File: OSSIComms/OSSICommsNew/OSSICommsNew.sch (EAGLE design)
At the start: 158 parts, among them Q2 NX-3215, U1 PCA9548APWR, U10 MAX6369, U11 OPA4347, U13 SN65HVD11QD, U14 LTC4411, U15 MCP1700_SOT23, U16 DS3231-L, U17 FM24V02-G, U18 TMP101, U19 24LC256-8LEAD, U2 ADG708, U20 LTC4411, U21 SN74LVC8T245PWR, U23 ADXRS450SOIC, U3 MAX890L, U4 OPA4347, U5 MSP430F1611, U6 OPA4347, U7 TPS3838, U8 ADG708, U9 ADR121, X1 ESQ-126-38-G-D, X2 JTAG10PINMINI-H, X3 MOLEX-22-05-7045, X5 P-PAD-S, X6 P-PAD-S

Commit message: ossi comms new added
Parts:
- removed BAT1: BATTERY-BH32T, OSSI:BATTERY-BH32T
- removed D1: MMSD4148T1G, OSSI:MMSD4148T1G
- removed R44, R58, R60, R64, R65: 470k, OSSI:R0603(1608)
- removed R45, R52, R57, R59, R61, R63, R66: 4.7k, OSSI:R0603(1608)
- removed R46, R47, R48, R49, R50, R51, R53, R54, R55, R69, R70: 1.5k, OSSI:R0603(1608)
- removed R56, R62, R68, R71, R72, R73: 10k, OSSI:R0603(1608)
- removed R67: 300k, OSSI:R0603(1608)
- removed R74: 100k, OSSI:R0603(1608)
- removed R76, R77: 0, OSSI:R0603(1608)
- removed TR2: FDV301N, OSSI:FDV301N
- removed U13: SN65HVD11QD, OSSI:SN65HVD11QD
- removed U15: MCP1700_SOT23, OSSI:MCP1700_SOT23
- removed U17: FM24V02-G, OSSI:FM24V02-G
- removed U18: TMP101, OSSI:TMP101
- removed U19: 24LC256-8LEAD, OSSI:24LC256-8LEAD
- removed U20: LTC4411, OSSI:LTC4411
- removed U21: SN74LVC8T245PWR, OSSI:SN74LVC8T245PWR
- removed U23: ADXRS450SOIC, OSSI:ADXRS450SOIC
- added C35, C44, C47, C55, C65, C67, C68, C70, C71: 100nF, OSSI:C0603(1608)
- added C43, C46: 1.2nF, OSSI:C0603(1608)
- added C45, C48, C54, C63, C74, C75, C87, C88, C89, C96: 10nF, OSSI:C0603(1608)
- added C49: 6.8pF, OSSI:C0603(1608)
- added C50, C51, C56, C57, C66: DNP, OSSI:C0603(1608)
- added C52, C53, C69: (no value), OSSI:C0603(1608)
- added C58, C72: 22uF,1210, OSSI:C1210(3225)-GCM32
- added C59, C60, C61: (no value), OSSI:C1210(3225)-GCM32
- added C62: 100uF,1210, OSSI:C0805(2012)
- added C64: 180pF, OSSI:C0603(1608)
- added C78, C79, C84: 22pF, OSSI:C0603(1608)
- added C80: 8.2pF, OSSI:C0603(1608)
- added C81: 47pF, OSSI:C0603(1608)
- added C82, C91, C95: 1nF, OSSI:C0603(1608)
- added C83, C90: 3.3uF, OSSI:C1210(3225)-TMK325
- added C85: 2pF, OSSI:C0603(1608)
- added C86: 56pF, OSSI:C0603(1608)
- added C92: 10pF, OSSI:C0603(1608)
- added C93: 15pF, OSSI:C0603(1608)
- added C94: 330pF, OSSI:C0603(1608)
- added JP2: (no value), OSSI:JP1Q
- added L10, L14, L15, L7, L8, L9: (no value), OSSI:L0603(1608)
- added L11: 3.9nH, OSSI:L0603(1608)
- added L12: 1.5nH, OSSI:L0603(1608)
- added L13: 0 Ohm, OSSI:L0805(2012)
- added L16: 330uH, OSSI:LLQH32CN
- added L2, L3: 11nH, OSSI:L0603(1608)
- added L4: 27nH, OSSI:L0603(1608)
- added L5: 39nH 3012, 1A rating, OSSI:LNR3012
- added L6: 47nH, OSSI:L0603(1608)
- added LED2: (no value), led:LEDCHIPLED_0603
- added TCXO2, TCXO3: 19.2MHz, OSSI:TCXO-M532
- added TP1: TP, OSSI:TP
- added TR1: FDV301N, OSSI:FDV301N
- added X7: 5268-03, OSSI:5268-03
- C11: value 100nF -> 470pF 0805; device OSSI:C0603(1608) -> OSSI:C0805(2012)
- C12: value 100nF -> 10uF; device OSSI:C0603(1608) -> OSSI:C1206(3216)-GCM31
- C15, C17, C19, C26, C28: value 100nF -> 10nF
- C2, C6: value 100nF -> 13pF
- C20, C31: value 100nF -> 22nF
- C23: value 100nF -> 100pF
- C29, C32: value 1uF 0805 -> 100nF; device OSSI:C0805(2012) -> OSSI:C0603(1608)
- C30: value 1uF 0805 -> 10nF; device OSSI:C0805(2012) -> OSSI:C0603(1608)
- C34: value 10uF, LDO Tantal 16V -> 100pF; device OSSI:C-TANTAL-A -> OSSI:C0603(1608)
- C37: value 10uF,3225 -> 100nF; device OSSI:C1210(3225)-GCM32 -> OSSI:C0603(1608)
- C38: value 4.7uF, 1210 -> 100pF; device OSSI:C1206(3216)-GCM31 -> OSSI:C0603(1608)
- C39: value 100nF -> 15pF
- C4, C5: value 100nF -> 10uF, LDO Tantal 16V; device OSSI:C0603(1608) -> OSSI:C-TANTAL-A
- C40: value 100nF -> 8.2pF
- C41: value 100nF -> 12pF
- C42: value 10uF, LDO Tantal 16V -> 8.2pF; device OSSI:C-TANTAL-A -> OSSI:C0603(1608)
- C9: value 100nF -> 1500pF
- F1: value POLYSWITCH -> LFCN-530; device OSSI:POLYSWITCH -> OSSI:LFCN-160
- L1: value 470uH, 240mA -> 26nH; device OSSI:LQH55 -> OSSI:L0603(1608)
- LED1: device SparkFun:LED0603 -> led:LEDCHIPLED_0603
- R10: value 10k -> 3.6k
- R11: value 10k -> 3.9
- R12: value 33k -> 1.1k
- R13: value 33k -> 3.6k
- R14: value 100k -> 3.9
- R15, R17: value 100k -> 280
- R16, R18: value 100k -> 100
- R19, R6, R7: value 100k -> 1.5k
- R21: value 10k -> 15.968k
- R22: value 250 -> 49.9k
- R23: value 250 -> 4.12k
- R24: value 250 -> TBD
- R25, R33: value 250 -> 1.5k
- R28, R32: value 250 -> 100k
- R29: value 250 -> 1k
- R34: value 4.7k -> 180
- R35: value 120, DNP -> 470k
- R36: value 10k -> 11nH
- R37: value 10k -> 22k
- R38: value 10k -> 100k
- R39: value 10k -> 1k
- R4: value 100k -> 470k
- R40, R5: value 10k -> 4.7k
- R41, R43: value 100k -> 4.7k
- R42: value 1.5k -> 4.7k
- R9: value 100k -> 1.1k
- U1: value PCA9548APWR -> MAX890L; device OSSI:PCA9548APWR -> OSSI:MAX890L
- U10: value MAX6369 -> LMZ10503EXT; device OSSI:MAX6369 -> OSSI:LMZ10503EXT
- U11: value OPA4347 -> OPA347; device OSSI:OPA4347 -> OSSI:OPA347
- U14: value LTC4411 -> RF5110G; device OSSI:LTC4411 -> OSSI:RF5110G
- U16: value DS3231-L -> MAX2640; device OSSI:DS3231-L -> OSSI:MAX2640
- U2: value ADG708 -> ADF7021-N; device OSSI:ADG708 -> OSSI:ADF7021-N
- U3: value MAX890L -> ADF7021-N; device OSSI:MAX890L -> OSSI:ADF7021-N
- U4: value OPA4347 -> PE4259; device OSSI:OPA4347 -> OSSI:PE4259
- U6: value OPA4347 -> MAX6369; device OSSI:OPA4347 -> OSSI:MAX6369
- U8: value ADG708 -> MCP1700_SOT23; device OSSI:ADG708 -> OSSI:MCP1700_SOT23
- U9: value ADR121 -> MAX869L; device OSSI:ADR127BUJZ-REEL7 -> OSSI:MAX869L
- X3: value MOLEX-22-05-7045 -> P-PAD-S; device OSSI:MOLEX-22-05-7045 -> OSSI:P-PAD-S
- X4: value (none) -> P-PAD-S; device OSSI:M03PTH -> OSSI:P-PAD-S
- X5: value P-PAD-S -> RFCON-MCX-R/A; device OSSI:P-PAD-S -> OSSI:RFCON-MCX-R/A
- X6: value P-PAD-S -> (none); device OSSI:P-PAD-S -> OSSI:M03PTH
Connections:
- net RESETOBC renamed /RST
- removed net /RE: R12.1, TR2.D, U13.P$2
- removed net 3.3VOBC_I2C: C18.1, C19.1, C20.1, C21.1, R5.2, R64.2, R65.1, R72.2, U14.P$5, U16.P$2, U17.A0, U17.VDD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
- removed net A: R35.2, U13.P$6, X3.2
- removed net ADC0: C5.1, R10.1, U5.59
- removed net ADC1: C9.1, R11.1, U5.60
- removed net B: R35.1, U13.P$7, X3.3
- removed net BAT_-CHRG_IN: R48.2, U5.17
- removed net BAT_-FAULT_IN: R49.2, U5.16
- removed net BAT_-ON_IN: R46.2, U5.19
- removed net BEACON_-FAULT_IN: R59.2, U5.22
- removed net BEACON_OFF_OUT: R54.2, U5.38
- removed net COMMS_-FAULT_IN: R61.2, U5.21
- removed net COMMS_OFF_OUT: R55.2, U5.37
- removed net DE: R13.2, U13.P$3, U5.48
- removed net GYRO_-CS: U23.P$4, U5.44
- removed net GYRO_SCLK: U23.P$16, U5.47
- removed net GYRO_SI: U23.P$15, U5.45
- removed net GYRO_SO: U23.P$5, U5.46
- removed net I2C_-RST: R4.1, U1.P$3, U5.28
- removed net I2C_SCL: R26.1, R30.1, U1.P$22
- removed net I2C_SCL_TP: R26.2, U5.31, X4.2
- removed net I2C_SDA: R27.1, R31.1, U1.P$23
- removed net I2C_SDA_TP: R27.2, U5.29, X4.1
- removed net IO_-OE: R43.1, U21.P$22, U5.24
- removed net LED_-FAULT_IN: R57.2, U5.23
- removed net LED_OFF_OUT: R53.2, U5.39
- removed net MUX_A0: R76.2, U2.P$1, U8.P$1
- removed net MUX_A1: R77.2, U2.P$16, U8.P$16
- removed net MUX_A2: U2.P$15, U5.51, U8.P$15
- removed net N$2 (its old number): R7.1, R9.2, U4A.+IN
- removed net N$666: C3.1, C34.+, U15.3, U3.P$6, U3.P$7
- removed net N$82: D1.A, L1.2, U23.P$8
- removed net N$90: C31.2, D1.C, U23.P$9
- removed net OBC_I2C_OFF: R74.1, U14.P$3, U5.30
- removed net OBC_SCL: R23.1, R24.1, R28.1, R33.1, R72.1, U1.P$14
- removed net OBC_SDA: R22.1, R25.1, R29.1, R32.1, R5.1, U1.P$13
- removed net OBC_WT_RST: C4.1, U10.P$7, U7.P$3
- removed net RTC_-INT: R64.1, U16.P$3, U5.26
- removed net RXD1: R34.1, U5.35
- removed net SCCHG_EN_OUT: R69.2, U5.41
- removed net SCOUT_-PG_IN: R51.2, U5.14
- removed net SCOUT_EN_OUT: R70.2, U5.40
- removed net SC_-ON_IN: R47.2, U5.18
- removed net SC_-PFO_IN: R50.2, U5.15
- removed net SOLAR_-ON_IN: R42.2, U5.20
- removed net STATUS_LED: JP1.2, LED1.A, R66.1
- removed net SUN_IN: U11B.-IN, U11B.OUT, U8.P$11
- removed net TEMP_-ALERT: R65.2, U18.3, U5.27
- removed net TXD1: R63.1, U5.34
- removed net VEXT: C37.1, F1.P$2, R6.1, U20.P$1
- removed net VEXT_OFF: R20.1, U20.P$3, U5.36
- removed net VREF_EXT: C33.2, U5.10, U9.P$4
- new net 3.3VCOMMS: C5.+, C54.1, C7.1, C70.1, C72.1, C8.1, L13.1, R2.2, R28.1, R30.2, R31.2, R4.2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
- new net COMMSRX_CE: U3.P$24, U5.21
- new net COMMSRX_CLK: R42.2, U3.P$35
- new net COMMSRX_CLKOUT: U3.P$36
- new net COMMSRX_CPOUT: C45.1, R15.2, R16.2, U3.P$42
- new net COMMSRX_DATA: R43.2, U3.P$34
- new net COMMSRX_MUXOUT: U3.P$37, U5.13
- new net COMMSRX_RFIN: C2.1, L4.2, U3.P$6
- new net COMMSRX_RFINB: C49.1, L4.1, U3.P$7
- new net COMMSRX_SCLK: U3.P$28, U5.17
- new net COMMSRX_SDATA: U3.P$26, U5.19
- new net COMMSRX_SLE: U3.P$25, U5.20
- new net COMMSRX_SREAD: U3.P$27, U5.18
- new net COMMSRX_SWD: U3.P$33, U5.16
- new net COMMSRX_TCXO: C79.2, U3.P$39
- new net COMMSRX_VCOIN: C43.1, R15.1, U3.P$1
- new net COMMSTX_CE: U2.P$24, U5.37
- new net COMMSTX_CLK: R41.2, U2.P$35
- new net COMMSTX_CLKOUT: U2.P$36
- new net COMMSTX_CPOUT: C48.1, R17.2, R18.2, U2.P$42
- new net COMMSTX_DATA: R40.2, U2.P$34
- new net COMMSTX_MUXOUT: U2.P$37, U5.22
- new net COMMSTX_RFOUT: C6.1, L1.1, U2.P$4
- new net COMMSTX_SCLK: U2.P$28, U5.25
- new net COMMSTX_SDATA: U2.P$26, U5.27
- new net COMMSTX_SLE: U2.P$25, U5.36
- new net COMMSTX_SREAD: U2.P$27, U5.26
- new net COMMSTX_TCXO: C78.2, U2.P$39
- new net COMMSTX_VCOIN: C46.1, R17.1, U2.P$1
- new net COMMS_-RST: C71.1, U6.P$7, U7.P$3
- new net LED1: R39.1, U5.50
- new net N$23: C51.2, L7.2, L8.1
- new net N$63: R43.1, U5.15
- new net N$66: C79.1, TCXO3.P$3
- new net N$67: R40.1, U5.24
- new net N$68: C78.1, TCXO2.P$3
- new net N$69: U5.42, U6.P$1
- new net N$73: C80.2, U14.P$3
- new net N$74: C5.-, R75.1
- new net N$75: L11.1, L5.1, U14.P$10, U14.P$11, U14.P$12, U14.P$9
- new net N$76: JP1.2, U11.OUT
- new net N$77: U5.33, X3.P$1
- new net N$78: U5.32, X4.P$1
- new net N$79: C93.1, L12.1, L16.2
- new net N$80: R36.1, U14.P$1
- new net OBC_-FAULT_IN: R5.1, U5.12
- new net OBC_OFF_OUT: R7.1, U5.2
- new net PA_-FAULT: R28.2, U9.P$10
- new net PA_BIAS: R33.1, R37.2, R38.1, U5.5
- new net PA_ON: R25.2, R35.1, U5.40
- new net RX_ON: U5.39
- new net STRUT_GND: H1.MOUNT
- new net TX_ON: R32.2, R6.1, U5.38
- new net VAPC: C88.2, C89.2, JP1.1, U14.P$15, U14.P$16
- new net VCCRF: C11.1, C12.1, C15.1, C17.1, C19.1, C22.1, C23.1, C24.1, C26.1, C28.1, C30.1, C33.1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
- new net VCOMMS_PA: C59.1, C60.1, C62.1, C64.1, C68.1, C81.1, C82.1, C83.1, C87.2, C90.1, C91.1, C92.1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
- net 3.3VOBC: no longer C11.1, C12.1, C15.1, C16.1, C17.2, C2.1, C27.1, C28.1, C30.1, C42.+, C6.1, C7.1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
- net ANT_DEPLOY1: no longer R45.1
- net ANT_DEPLOY2: no longer R52.1
- net BAT_-CHRG: no longer U21.P$18
- net BAT_-FAULT: no longer U21.P$17
- net BAT_-ON: no longer U21.P$20
- net BAT_TEMP: no longer R68.2
- net BEACON_-FAULT: no longer R58.1, R59.1
- net BEACON_OFF: no longer R54.1
- net BEACON_SCL: no longer U1.P$7
- net BEACON_SDA: no longer U1.P$6
- net BUS_CS: no longer R40.2
- net COMMS_-FAULT: now also U1.P$8; no longer R60.1, R61.1
- net COMMS_OFF: now also C1.1, R3.2, U1.P$3; no longer R55.1
- net COMMS_SCL: now also R26.1, R30.1, X6.2; no longer U1.P$5
- net COMMS_SDA: now also R27.1, R31.1, X6.1; no longer U1.P$4
- net GND: now also C17.2, C33.2, C34.2, C35.2, C4.-, C42.2, C43.2, C44.2, C45.2, C46.2, C47.2, C48.2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; no longer BAT1.-, C17.1, C2.2, C20.2, C21.2, C31.1, C32.2, C33.1, C34.-, C39.2, C4.2, C5.2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
- net LED_-FAULT: no longer R44.1, R57.1
- net LED_OFF: no longer R53.1
- net LED_SCL: no longer U1.P$9
- net LED_SDA: no longer U1.P$8
- net N$1: now also C16.1, U3.P$41; no longer U10.P$1, U5.12
- net N$10: now also C25.1, U3.P$11; no longer R1.2, U3.P$5
- net N$11: now also C3.1, C4.+, U1.P$6, U1.P$7, U8.3; no longer U2.P$4, U4D.-IN, U4D.OUT
- net N$12: now also R1.2, U1.P$5; no longer U6A.-IN, U6A.OUT, U8.P$7
- net N$14: now also C39.2, U16.4; no longer R34.2, U13.P$1
- net N$15: now also C50.1, F1.P$1, L9.1; no longer R33.2, U16.P$16
- net N$16: now also C9.2, F1.P$3; no longer R73.1, U1.P$15, U1.P$16, U1.P$17, U1.P$18, U1.P$19, U1.P$20
- net N$21: now also C53.1, L10.1, L9.2; no longer U6B.-IN, U6B.OUT, U8.P$6
- net N$22: now also C20.1, U3.P$48; no longer R63.2, U13.P$4
- net N$24: now also R9.1, U3.P$8; no longer R14.1, R15.2, U4B.+IN
- net N$25: now also R10.1, U3.P$10; no longer R16.1, R17.2, U4C.+IN
- net N$26: now also C21.2, R11.2; no longer R18.1, R19.2, U4D.+IN
- net N$27: now also C31.1, U2.P$48; no longer R11.2, U2.P$8
- net N$28: now also R13.2, U2.P$10; no longer U6C.-IN, U6C.OUT, U8.P$5
- net N$29: now also C32.2, R14.2; no longer R10.2, U8.P$8
- net N$3: now also C36.1, U2.P$11; no longer U2.P$7, U4A.-IN, U4A.OUT
- net N$30: now also R12.2, U2.P$8; no longer U6D.-IN, U6D.OUT, U8.P$4
- net N$31: now also C27.1, U2.P$41; no longer U11A.-IN, U11A.OUT, U8.P$12
- net N$32: now also C29.1, U2.P$31; no longer R66.2, U5.13
- net N$33: now also C42.1, C80.1, L3.2, R34.2; no longer C32.1, U23.P$1
- net N$34: now also C31.2, C32.1, U2.P$2; no longer R29.2, U19.P$5
- net N$35: now also C20.2, C21.1, U3.P$2; no longer R28.2, U19.P$6
- net N$36: now also C40.1, C6.2, L2.1; no longer R25.2, U17.SDA
- net N$37: now also C41.1, L2.2, L3.1; no longer R45.2, U5.43
- net N$38: now also C47.1, R18.1; no longer R52.2, U5.42
- net N$39: now also C52.2, C57.2, L8.2; no longer R24.2, U17.SCL
- net N$4: now also C56.2, C86.2, L7.1; no longer R41.1, R6.2, TR2.G
- net N$40: now also C44.1, R16.1; no longer R22.2, U18.6
- net N$41: now also C69.2, U4.P$5; no longer R23.2, U18.1
- net N$42: now also R6.2, U4.P$4; no longer R67.2, U5.25
- net N$43: now also C39.1, L14.2, L15.1; no longer C36.1, F1.P$1, X3.1
- net N$44: now also R19.1, U4.P$6; no longer U11C.-IN, U11C.OUT, U8.P$10
- net N$45: now also LED2.A, R29.2; no longer U11D.-IN, U11D.OUT, U8.P$9
- net N$46: now also C69.1, X5.1; no longer C29.1, U23.P$14
- net N$47: now also C65.1, R20.1, TR1.D, U9.P$7; no longer C41.1, R71.1, U11D.+IN
- net N$48: now also R29.1, U5.49; no longer C40.1, R68.1, U11C.+IN
- net N$49: now also JP2.1, LED1.A, R39.2; no longer R48.1, U21.P$6
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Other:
- note added: "0.8Vpp out with ac coupled capacitor"
- note added: "0dbm"
- note added: "1Watt"
- note added: "50 Ohm"
- note added: "75 Ohm"
- note added: "C value?"
- note added: "DIGITAL / RF POWER CHOKE"
- note added: "Harmonics Filter"
- note added: "LC Balun"
- note added: "Maching"
- note added: "OPEN SOURSE SATELLITE INITIATIVE Ver 0.9"
- note added: "PA Maching"
- note added: "Power Amplifier"
- note added: "Tantal Cap should be used"
- note added: "Use DAC to change the divider voltage point"
- note added: "also check 23.7k / 75k combination"
- note added: "chage this if resistance affects"
- note added: "clkout testpoint"
- note added: "for VAPC of PA"
- note added: "important!!"
- note added: "post impedance matching"
- note added: "pull down!!"
- note added: "set to 2.8V"
- note added: "sync word detection eyediagram test?"
- note added: "unconnected pins?"
- note added: "variable capacitor"
- note removed: "/RE needs to go LOW when external interface connector is inserted"
- note removed: "12pF"
- note removed: "60s time set"
- note removed: "All pull up to VBUS"
- note removed: "But can be turned off by OBC for testing"
- note removed: "DE pin to OBC"
- note removed: "EN is Active High"
- note removed: "Max Current: 1.2A"
- note removed: "OBC pull high DE pin when TX"
- note removed: "ROSC for better DCO"
- note removed: "Ref1: Poly Sat paper"
- note removed: "Ref2: Pumpkin Co. Cubesat kit"
- note removed: "Remove 0 Ohm for SMCLK / ACLK out"
- note removed: "VEXT On by default to charge the battery from VEXT"
- note removed: "VEXT will turn on the 485 in Receiver mode"
- note removed: "Vout Overshoot check"
- note removed: "changed from 0 -> 1k"
- note removed: "critical signal should be directly connect to MCU"
- note removed: "input to OBC"
- note removed: "interface side select power from Solar or 5V adaptor"
- note removed: "led"
- note removed: "output capacitor!"
- note removed: "output capacitor!!!"
- note removed: "output from OBC"
- note removed: "power capacitors"
- note removed: "put 1k resistor at the output of current sensor"
- note removed: "sun sensor"
- note removed: "unused pins!!"
- note removed: "write enabled"

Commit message: beta 1 release
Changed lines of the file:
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@@
 <part name="GND60" library="OSSI" deviceset="GND" device=""/>
 <part name="3.3VCOMMS17" library="OSSI" deviceset="3.3VCOMMS" device=""/>
-<part name="VCCRF1" library="OSSI" deviceset="VCCRF" device=""/>
 <part name="VCCRF3" library="OSSI" deviceset="VCCRF" device=""/>
 <part name="VCCRF4" library="OSSI" deviceset="VCCRF" device=""/>
@@
 <instance part="GND58" gate="1" x="220.98" y="210.82"/>
 <instance part="GND59" gate="1" x="220.98" y="76.2"/>
-<instance part="VCCRF1" gate="G$1" x="17.78" y="149.86"/>
 <instance part="VCCRF5" gate="G$1" x="101.6" y="81.28"/>
 <instance part="VCCRF6" gate="G$1" x="261.62" y="71.12"/>

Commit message: schematics renumbered
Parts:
- removed C94: 330pF, OSSI:C0603(1608)
- removed C95: 1nF, OSSI:C0603(1608)
- removed C96: 10nF, OSSI:C0603(1608)
- removed R75: 0, OSSI:R0603(1608)
- removed U14: RF5110G, OSSI:RF5110G
- removed U16: MAX2640, OSSI:MAX2640
- added C73, C77: 100nF, OSSI:C0603(1608)
- added C76: 10nF, OSSI:C0603(1608)
- added R44: 100k, OSSI:R0603(1608)
- added U12: MAX890L, OSSI:MAX890L
- added U13: MCP1700_SOT23, OSSI:MCP1700_SOT23
- C1: value 1uF -> 6.8pF
- C10: value 100nF -> (none)
- C11: value 470pF 0805 -> 3.3uF; device OSSI:C0805(2012) -> OSSI:C1210(3225)-TMK325
- C12: value 10uF -> 10pF; device OSSI:C1206(3216)-GCM31 -> OSSI:C0603(1608)
- C13: value 12.5pF -> 1nF
- C14: value 12.5pF -> 15pF
- C15: value 10nF -> (none)
- C16: value 100nF -> DNP
- C17: value 10nF -> DNP
- C18, C25: value 100nF -> 8.2pF
- C19: value 10nF -> 12pF
- C2: value 13pF -> DNP
- C20: value 22nF -> 8.2pF
- C21: value 100nF -> 22pF
- C22: value 100nF -> 2pF
- C23: value 100pF -> DNP
- C24, C3: value 100nF -> 13pF
- C26: value 10nF -> 56pF
- C27: value 100nF -> 330pF
- C29, C70: value 100nF -> 100pF
- C30: value 10nF -> 47pF
- C31: value 22nF -> 1nF
- C32, C35, C36, C67: value 100nF -> 10nF
- C33: value 100nF -> 1nF
- C34: value 100pF -> 100nF
- C37: value 100nF -> 3.3uF; device OSSI:C0603(1608) -> OSSI:C1210(3225)-TMK325
- C38: value 100pF -> 180pF
- C39, C93: value 15pF -> 100nF
- C4: value 10uF, LDO Tantal 16V -> 15pF; device OSSI:C-TANTAL-A -> OSSI:C0603(1608)
- C40: value 8.2pF -> 100nF
- C41: value 12pF -> (none); device OSSI:C0603(1608) -> OSSI:C1210(3225)-GCM32
- C42: value 8.2pF -> 22uF,1210; device OSSI:C0603(1608) -> OSSI:C1210(3225)-GCM32
- C43: value 1.2nF -> 10nF
- C44: value 100nF -> 100uF,1210; device OSSI:C0603(1608) -> OSSI:C0805(2012)
- C45: value 10nF -> (none); device OSSI:C0603(1608) -> OSSI:C1210(3225)-GCM32
- C46: value 1.2nF -> (none); device OSSI:C0603(1608) -> OSSI:C1210(3225)-GCM32
- C48, C54, C88: value 10nF -> 100nF
- C49: value 6.8pF -> 100nF
- C5: value 10uF, LDO Tantal 16V -> DNP; device OSSI:C-TANTAL-A -> OSSI:C0603(1608)
- C50, C66: value DNP -> 100nF
- C51, C56: value DNP -> 10nF
- C52, C69: value (none) -> 100nF
- C53: value (none) -> 100pF
- C55, C71: value 100nF -> 22nF
- C57: value DNP -> 1.2nF
- C58: value 22uF,1210 -> 100nF; device OSSI:C1210(3225)-GCM32 -> OSSI:C0603(1608)
- C59: value (none) -> 10nF; device OSSI:C1210(3225)-GCM32 -> OSSI:C0603(1608)
- C6: value 13pF -> 10uF; device OSSI:C0603(1608) -> OSSI:C1206(3216)-GCM31
- C60: value (none) -> 100nF; device OSSI:C1210(3225)-GCM32 -> OSSI:C0603(1608)
- C61: value (none) -> 22pF; device OSSI:C1210(3225)-GCM32 -> OSSI:C0603(1608)
- C62: value 100uF,1210 -> 10nF; device OSSI:C0805(2012) -> OSSI:C0603(1608)
- C64: value 180pF -> 100nF
- C7: value 100nF -> 470pF 0805; device OSSI:C0603(1608) -> OSSI:C0805(2012)
- C72: value 22uF,1210 -> 1.2nF; device OSSI:C1210(3225)-GCM32 -> OSSI:C0603(1608)
- C79: value 22pF -> 10nF
- C8: value 100nF -> 1500pF
- C80: value 8.2pF -> 12.5pF
- C81: value 47pF -> 12.5pF
- C82: value 1nF -> 100nF
- C83: value 3.3uF -> 100nF; device OSSI:C1210(3225)-TMK325 -> OSSI:C0603(1608)
- C84: value 22pF -> 100nF
- C85: value 2pF -> 100nF
- C86: value 56pF -> 100nF
- C87: value 10nF -> 1uF
- C89: value 10nF -> 10uF, LDO Tantal 16V; device OSSI:C0603(1608) -> OSSI:C-TANTAL-A
- C9: value 1500pF -> (none)
- C90: value 3.3uF -> 10uF, LDO Tantal 16V; device OSSI:C1210(3225)-TMK325 -> OSSI:C-TANTAL-A
- C91: value 1nF -> 10nF
- C92: value 10pF -> 22uF,1210; device OSSI:C0603(1608) -> OSSI:C1210(3225)-GCM32
- L1: value 26nH -> 27nH
- L11: value 3.9nH -> 11nH
- L12: value 1.5nH -> 11nH
- L13: value 0 Ohm -> 3.9nH; device OSSI:L0805(2012) -> OSSI:L0603(1608)
- L14: value (none) -> 26nH
- L15: value (none) -> 39nH 3012, 1A rating; device OSSI:L0603(1608) -> OSSI:LNR3012
- L16: value 330uH -> 0 Ohm; device OSSI:LLQH32CN -> OSSI:L0805(2012)
- L2, L3: value 11nH -> (none)
- L4: value 27nH -> (none)
- L5: value 39nH 3012, 1A rating -> 47nH; device OSSI:LNR3012 -> OSSI:L0603(1608)
- L6: value 47nH -> (none)
- L7: value (none) -> 330uH; device OSSI:L0603(1608) -> OSSI:LLQH32CN
- L9: value (none) -> 1.5nH
- R1: value TBD -> 100k
- R10: value 3.6k -> 1.5k
- R11: value 3.9 -> TBD
- R12: value 1.1k -> 100k
- R13: value 3.6k -> 100k
- R14: value 3.9 -> 1.5k
- R15: value 280 -> 100k
- R16: value 100 -> 22k
- R17: value 280 -> 3.9
- R18: value 100 -> 3.6k
- R19: value 1.5k -> 1.1k
- R2, R3: value 100k -> 1.5k
- R20: value 100k -> 280
- R21: value 15.968k -> 100
- R22: value 49.9k -> 3.6k
- R23: value 4.12k -> 3.9
- R24: value TBD -> 1.1k
- R25: value 1.5k -> 280
- R26: value 250 -> 100
- R28: value 100k -> 4.7k
- R29: value 1k -> 4.7k
- R30: value 10k -> 250
- R32: value 100k -> 10k
- R33: value 1.5k -> 4.7k
- R34: value 180 -> 4.7k
- R35: value 470k -> 4.7k
- R36: value 11nH -> 470k
- R37: value 22k -> 1.5k
- R38: value 100k -> 1k
- R4: value 470k -> 180
- R41: value 4.7k -> 0
- R42: value 4.7k -> TBD
- R43: value 4.7k -> 100k
- R5: value 4.7k -> 11nH
- R6: value 1.5k -> 4.12k
- R7: value 1.5k -> 470k
- R8: value 4.7k -> 15.968k
- R9: value 1.1k -> 49.9k
- U1: value MAX890L -> MAX2640; device OSSI:MAX890L -> OSSI:MAX2640
- U10: value LMZ10503EXT -> MAX6369; device OSSI:LMZ10503EXT -> OSSI:MAX6369
- U11: value OPA347 -> TPS3838; device OSSI:OPA347 -> OSSI:TPS3838
- U2: value ADF7021-N -> PE4259; device OSSI:ADF7021-N -> OSSI:PE4259
- U3: value ADF7021-N -> RF5110G; device OSSI:ADF7021-N -> OSSI:RF5110G
- U4: value PE4259 -> OPA347; device OSSI:PE4259 -> OSSI:OPA347
- U5: value MSP430F1611 -> MAX869L; device OSSI:MSP430F1611 -> OSSI:MAX869L
- U6: value MAX6369 -> LMZ10503EXT; device OSSI:MAX6369 -> OSSI:LMZ10503EXT
- U7: value TPS3838 -> ADF7021-N; device OSSI:TPS3838 -> OSSI:ADF7021-N
- U8: value MCP1700_SOT23 -> ADF7021-N; device OSSI:MCP1700_SOT23 -> OSSI:ADF7021-N
- U9: value MAX869L -> MSP430F1611; device OSSI:MAX869L -> OSSI:MSP430F1611
- X2: value JTAG10PINMINI-H -> RFCON-MCX-R/A; device OSSI:JTAG10PINMINI-H -> OSSI:RFCON-MCX-R/A
- X3: value P-PAD-S -> (none); device OSSI:P-PAD-S -> OSSI:M03PTH
- X5: value RFCON-MCX-R/A -> 5268-03; device OSSI:RFCON-MCX-R/A -> OSSI:5268-03
- X6: value (none) -> P-PAD-S; device OSSI:M03PTH -> OSSI:P-PAD-S
- X7: value 5268-03 -> JTAG10PINMINI-H; device OSSI:5268-03 -> OSSI:JTAG10PINMINI-H
- renumbered Q2 to Q1, TCXO3 to TCXO1
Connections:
- net /RST: now also R40.2, R44.1, U11.P$4, U9.58; no longer R2.1, R8.2, U5.58, U7.P$4
- net 3.3VCOMMS: now also C84.1, C85.1, C86.1, C90.+, C91.1, C92.1, L16.1, R12.1, R32.2, R36.2, R44.2, U10.P$4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; no longer C5.+, C54.1, C7.1, C70.1, C72.1, C8.1, L13.1, R2.2, R28.1, R30.2, R4.2, U5.1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
- net COMMSRX_CE: now also U7.P$24, U9.21; no longer U3.P$24, U5.21
- net COMMSRX_CLK: now also R35.2, U7.P$35; no longer R42.2, U3.P$35
- net COMMSRX_CLKOUT: now also U7.P$36; no longer U3.P$36
- net COMMSRX_CPOUT: now also C62.1, R20.2, R21.2, U7.P$42; no longer C45.1, R15.2, R16.2, U3.P$42
- net COMMSRX_DATA: now also R34.2, U7.P$34; no longer R43.2, U3.P$34
- net COMMSRX_MUXOUT: now also U7.P$37, U9.13; no longer U3.P$37, U5.13
- net COMMSRX_RFIN: now also C3.1, L1.2, U7.P$6; no longer C2.1, L4.2, U3.P$6
- net COMMSRX_RFINB: now also C1.1, L1.1, U7.P$7; no longer C49.1, L4.1, U3.P$7
- net COMMSRX_SCLK: now also U7.P$28, U9.17; no longer U3.P$28, U5.17
- net COMMSRX_SDATA: now also U7.P$26, U9.19; no longer U3.P$26, U5.19
- net COMMSRX_SLE: now also U7.P$25, U9.20; no longer U3.P$25, U5.20
- net COMMSRX_SREAD: now also U7.P$27, U9.18; no longer U3.P$27, U5.18
- net COMMSRX_SWD: now also U7.P$33, U9.16; no longer U3.P$33, U5.16
- net COMMSRX_TCXO: now also C61.2, U7.P$39; no longer C79.2, U3.P$39
- net COMMSRX_VCOIN: now also C57.1, R20.1, U7.P$1; no longer C43.1, R15.1, U3.P$1
- net COMMSTX_CE: now also U8.P$24, U9.37; no longer U2.P$24, U5.37
- net COMMSTX_CLK: now also R28.2, U8.P$35; no longer R41.2, U2.P$35
- net COMMSTX_CLKOUT: now also U8.P$36; no longer U2.P$36
- net COMMSTX_CPOUT: now also C75.1, R25.2, R26.2, U8.P$42; no longer C48.1, R17.2, R18.2, U2.P$42
- net COMMSTX_DATA: now also R29.2, U8.P$34; no longer R40.2, U2.P$34
- net COMMSTX_MUXOUT: now also U8.P$37, U9.22; no longer U2.P$37, U5.22
- net COMMSTX_RFOUT: now also C24.1, L14.1, U8.P$4; no longer C6.1, L1.1, U2.P$4
- net COMMSTX_SCLK: now also U8.P$28, U9.25; no longer U2.P$28, U5.25
- net COMMSTX_SDATA: now also U8.P$26, U9.27; no longer U2.P$26, U5.27
- net COMMSTX_SLE: now also U8.P$25, U9.36; no longer U2.P$25, U5.36
- net COMMSTX_SREAD: now also U8.P$27, U9.26; no longer U2.P$27, U5.26
- net COMMSTX_TCXO: now also U8.P$39; no longer U2.P$39
- net COMMSTX_VCOIN: now also C72.1, R25.1, U8.P$1; no longer C46.1, R17.1, U2.P$1
- net COMMS_-FAULT: now also U12.P$8; no longer U1.P$8
- net COMMS_-RST: now also C83.1, U10.P$7, U11.P$3; no longer C71.1, U6.P$7, U7.P$3
- net COMMS_OFF: now also C87.1, R43.2, U12.P$3; no longer C1.1, R3.2, U1.P$3
- net COMMS_SCL: now also R32.1, X3.2; no longer R26.1, X6.2
- net COMMS_SDA: now also X3.1; no longer X6.1
- net GND: now also C16.1, C17.1, C2.2, C20.2, C21.2, C23.1, C28.1, C31.2, C32.1, C36.1, C39.2, C5.2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; no longer C10.2, C15.2, C16.2, C17.2, C23.2, C24.2, C25.2, C26.2, C28.2, C3.2, C36.2, C38.2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
- net LED1: now also U9.50; no longer U5.50
- net N$1: now also C60.1, U7.P$41; no longer C16.1, U3.P$41
- net N$10: now also C49.1, U7.P$11; no longer C25.1, U3.P$11
- net N$11: now also C88.1, C89.+, U12.P$6, U12.P$7, U13.3; no longer C3.1, C4.+, U1.P$6, U1.P$7, U8.3
- net N$12: now also R42.2, U12.P$5; no longer R1.2, U1.P$5
- net N$13: now also C82.1, U9.7; no longer C10.1, U5.7
- net N$14: now also C4.2, U1.4; no longer C39.2, U16.4
- net N$15: now also C5.1, L6.1; no longer C50.1, L9.1
- net N$16: now also C8.2; no longer C9.2
- net N$17: now also U9.57, X7.7; no longer U5.57, X2.7
- net N$18: now also U9.56, X7.5; no longer U5.56, X2.5
- net N$19: now also U9.55, X7.3; no longer U5.55, X2.3
- net N$2: now also R40.1, X7.10; no longer R8.1, X2.10
- net N$20: now also U9.54, X7.1; no longer U5.54, X2.1
- net N$21: now also C9.1, L4.1, L6.2; no longer C53.1, L10.1, L9.2
- net N$22: now also C55.1, U7.P$48; no longer C20.1, U3.P$48
- net N$23: now also C17.2, L10.2; no longer C51.2, L7.2
- net N$24: now also R19.1, U7.P$8; no longer R9.1, U3.P$8
- net N$25: now also R18.1, U7.P$10; no longer R10.1, U3.P$10
- net N$26: now also C54.2, R17.2; no longer C21.2, R11.2
- net N$27: now also C71.1, U8.P$48; no longer C31.1, U2.P$48
- net N$28: now also R22.2, U8.P$10; no longer R13.2, U2.P$10
- net N$29: now also C68.2, R23.2; no longer C32.2, R14.2
- net N$3: now also C65.1, U8.P$11; no longer C36.1, U2.P$11
- net N$30: now also R24.2, U8.P$8; no longer R12.2, U2.P$8
- net N$31: now also C77.1, U8.P$41; no longer C27.1, U2.P$41
- net N$32: now also C66.1, U8.P$31; no longer C29.1, U2.P$31
- net N$33: now also C20.1, C25.1, L12.2, R4.2; no longer C42.1, C80.1, L3.2, R34.2
- net N$34: now also C68.1, C71.2, U8.P$2; no longer C31.2, C32.1, U2.P$2
- net N$35: now also C54.1, C55.2, U7.P$2; no longer C20.2, C21.1, U3.P$2
- net N$36: now also C18.1, C24.2, L11.1; no longer C40.1, C6.2, L2.1
- net N$37: now also C19.1, L11.2, L12.1; no longer C41.1, L2.2, L3.1
- net N$38: now also C73.1, R26.1; no longer C47.1, R18.1
- net N$39: now also C15.2, C16.2; no longer C52.2, C57.2
- net N$4: now also C23.2, C26.2, L10.1; no longer C56.2, C86.2, L7.1
- net N$40: now also C58.1, R21.1; no longer C44.1, R16.1
- net N$41: now also C10.2, U2.P$5; no longer C69.2, U4.P$5
- net N$42: now also R2.2, U2.P$4; no longer R6.2, U4.P$4
- net N$43: now also C4.1, L2.1, L3.2; no longer C39.1, L14.2, L15.1
- net N$44: now also R3.1, U2.P$6; no longer R19.1, U4.P$6
- net N$45: now also LED1.A, R38.2; no longer LED2.A, R29.2
- net N$46: now also C10.1, X2.1; no longer C69.1, X5.1
- net N$47: now also C40.1, R15.1, U5.P$7; no longer C65.1, R20.1, U9.P$7
- net N$48: now also R38.1, U9.49; no longer R29.1, U5.49
- net N$49: now also LED2.A; no longer LED1.A
- net N$5: now also C81.1, U9.8; no longer C13.1, U5.8
- net N$50: now also C43.1, U6.P$3; no longer C63.1, U10.P$3
- net N$51: now also R10.1; no longer R25.1
- net N$52: now also C41.1, C42.1, U5.P$11, U5.P$14, U5.P$15, U5.P$2, U5.P$3, U5.P$6, U6.P$1, U6.P$2; no longer C58.1, C61.1, U10.P$1, U10.P$2, U9.P$11, U9.P$14, U9.P$15, U9.P$2, U9.P$3, U9.P$6
- net N$53: now also R6.2, R8.1, R9.2, U6.P$5; no longer R21.1, R22.2, R23.2, U10.P$5
- net N$54: now also C38.2, R6.1; no longer C64.2, R23.1
- net N$55: now also R11.2, U5.P$9; no longer R24.2, U9.P$9
- net N$56: now also U9.35, X5.3; no longer U5.35, X7.3
- net N$57: now also U9.34, X5.2; no longer U5.34, X7.2
- net N$58: now also C15.1, U2.P$1; no longer C52.1, U4.P$1
- net N$59: now also C9.2, U2.P$3; no longer C53.2, U4.P$3
- net N$6: now also C80.1, U9.9; no longer C14.1, U5.9
- net N$60: now also U9.29; no longer U5.29
- net N$61: now also R30.2, U9.31; no longer R26.2, U5.31
- net N$62: now also C2.1, C3.2, L3.1; no longer C2.2, C66.1, L14.1
- net N$63: now also R34.1, U9.15; no longer R43.1, U5.15
- net N$64: now also R35.1, U9.14; no longer R42.1, U5.14
- net N$65: now also R28.1, U9.23; no longer R41.1, U5.23
- net N$66: now also C61.1; no longer C79.1
- net N$67: now also R29.1, U9.24; no longer R40.1, U5.24
- net N$69: now also U10.P$1, U9.42; no longer U5.42, U6.P$1
- net N$7: now also L5.1, U1.1; no longer L6.1, U16.1
- net N$70: now also C39.1, R14.2, U4.+IN; no longer C67.1, R33.2, U11.+IN
- net N$71: now also C21.1, C22.1, C26.1, L13.2; no longer C84.1, C85.1, C86.1, L11.2
- net N$72: now also L9.2, U3.P$5, U3.P$6; no longer L12.2, U14.P$5, U14.P$6
- net N$73: now also C25.2, U3.P$3; no longer C80.2, U14.P$3
- net N$74: now also C90.-, R41.1; no longer C5.-, R75.1
- net N$75: now also L13.1, L15.1, U3.P$10, U3.P$11, U3.P$12, U3.P$9; no longer L11.1, L5.1, U14.P$10, U14.P$11, U14.P$12, U14.P$9
- net N$76: now also U4.OUT; no longer U11.OUT
- net N$77: now also U9.33, X6.P$1; no longer U5.33, X3.P$1
- net N$78: now also U9.32; no longer U5.32
- net N$79: now also C14.1, L7.2, L9.1; no longer C93.1, L12.1, L16.2
- net N$8: now also C8.1, L5.2; no longer C9.1, L6.2
- net N$80: now also R5.1, U3.P$1; no longer R36.1, U14.P$1
- net N$9: now also C50.1, U7.P$31; no longer C18.1, U3.P$31
- net OBC_-FAULT: now also R33.2, R36.1; no longer R4.1, R5.2
- net OBC_-FAULT_IN: now also R33.1, U9.12; no longer R5.1, U5.12
- net OBC_OFF: now also R37.2; no longer R7.2
- net OBC_OFF_OUT: now also R37.1, U9.2; no longer R7.1, U5.2
- net PA_-FAULT: now also R12.2, U5.P$10; no longer R28.2, U9.P$10
- net PA_BIAS: now also R13.1, R14.1, R16.2, U9.5; no longer R33.1, R37.2, R38.1, U5.5
- net PA_ON: now also R10.2, R7.1, U9.40; no longer R25.2, R35.1, U5.40
- net RX_ON: now also U9.39; no longer U5.39
- net STRUT_GND: now also H4.MOUNT; no longer H1.MOUNT
- net TX_ON: now also R1.2, R2.1, U9.38; no longer R32.2, R6.1, U5.38
- net VAPC: now also C28.2, C32.2, U3.P$15, U3.P$16; no longer C88.2, C89.2, U14.P$15, U14.P$16
- net VBUS: now also R15.2, U12.P$1, U12.P$2, U5.P$1, U5.P$12, U5.P$13, U5.P$16, U5.P$4, U5.P$5; no longer R20.2, U1.P$1, U1.P$2, U9.P$1, U9.P$12, U9.P$13, U9.P$16, U9.P$4, U9.P$5
- net VCCRF: now also C29.1, C48.1, C51.1, C52.1, C53.1, C56.1, C59.1, C6.1, C63.1, C64.1, C67.1, C69.1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; no longer C11.1, C12.1, C15.1, C17.1, C19.1, C22.1, C23.1, C24.1, C26.1, C28.1, C30.1, C33.1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
- net VCOMMS_PA: now also C11.1, C12.1, C13.1, C27.1, C30.1, C31.1, C33.1, C35.1, C36.2, C37.1, C38.1, C44.1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; no longer C59.1, C60.1, C62.1, C64.1, C68.1, C81.1, C82.1, C83.1, C87.2, C90.1, C91.1, C92.1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

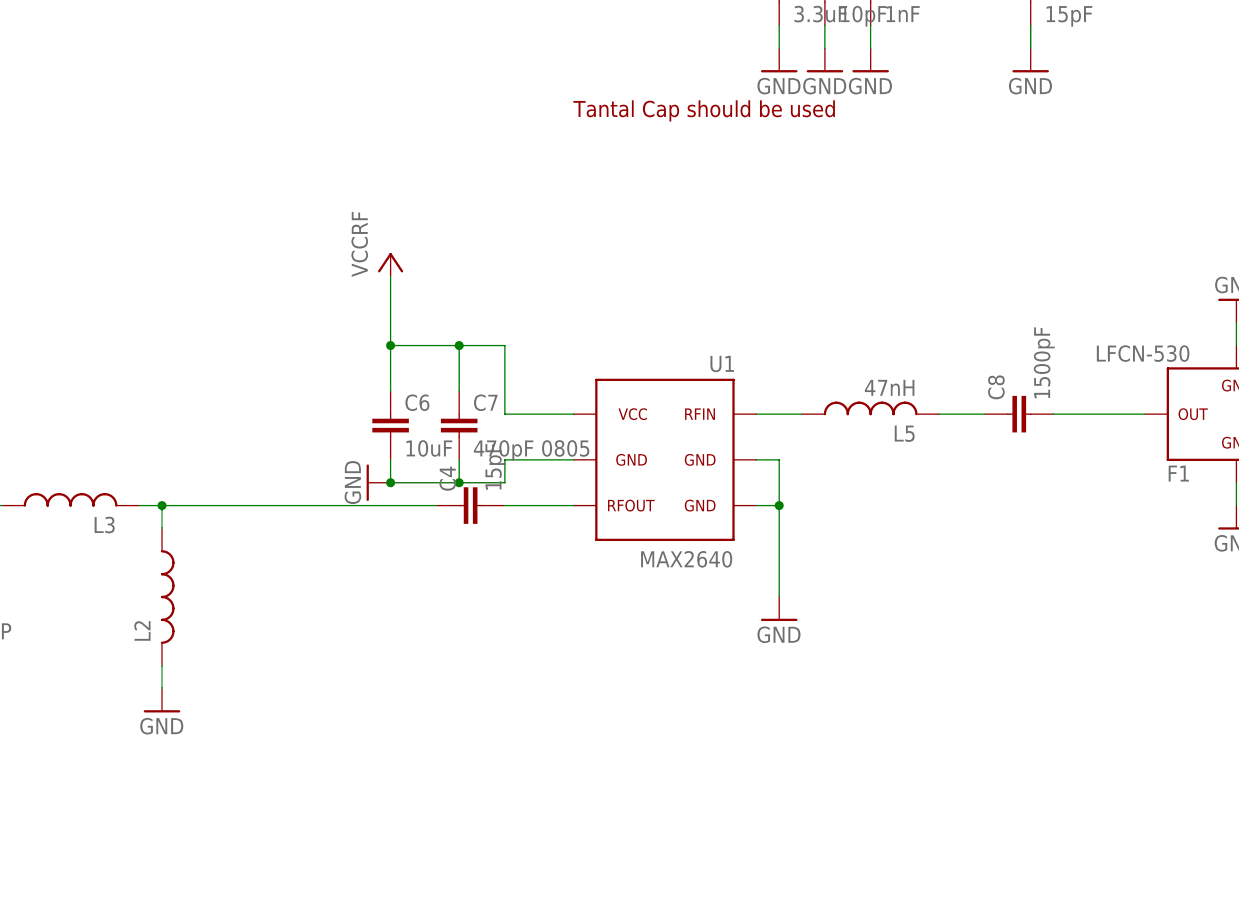
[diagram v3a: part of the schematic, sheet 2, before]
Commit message: LNA gain measured to 15.5dB and R / L values are fixed
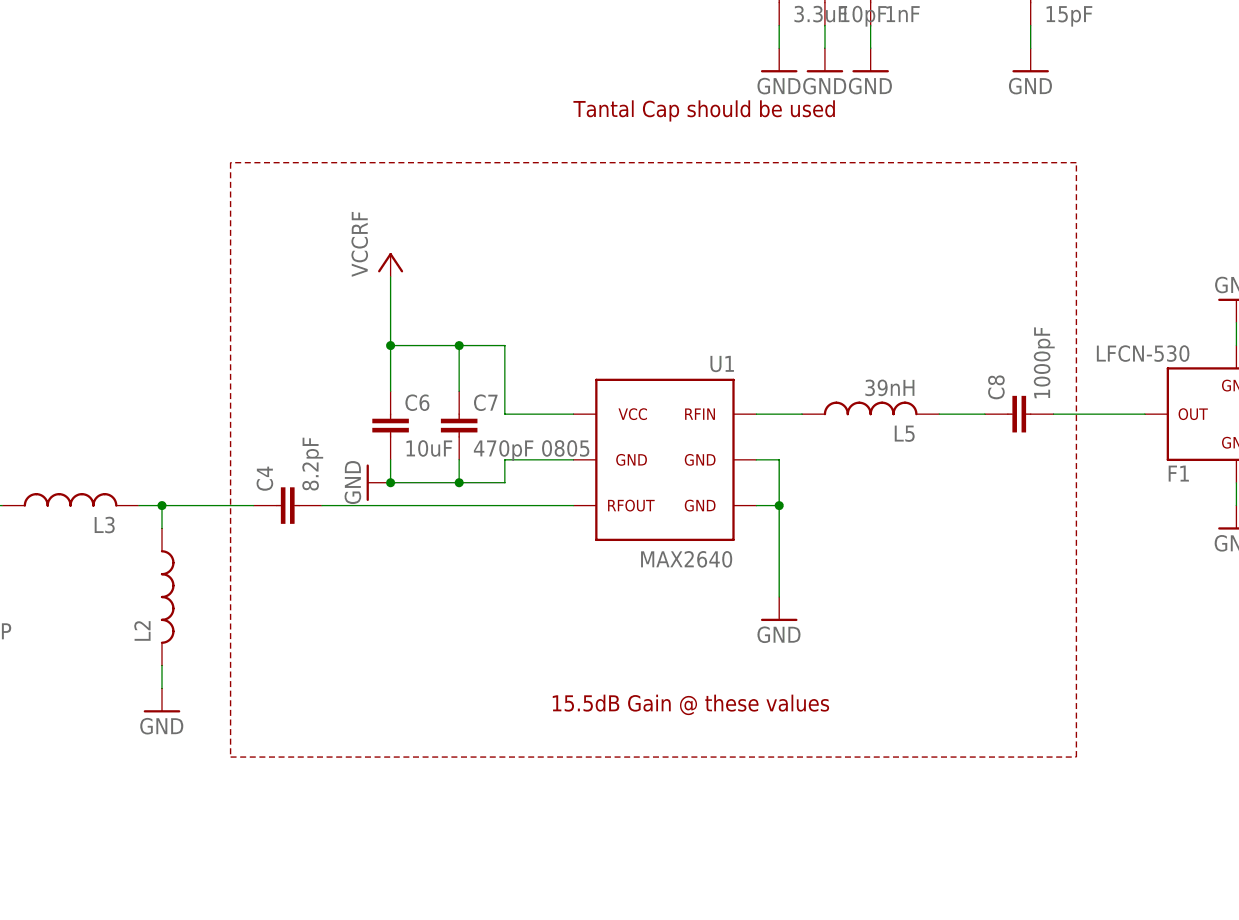
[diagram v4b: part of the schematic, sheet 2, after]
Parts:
- C4: value 15pF -> 8.2pF
- C8: value 1500pF -> 1000pF
- L5: value 47nH -> 39nH
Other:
- note added: "15.5dB Gain @ these values"
- moved on the sheet: C4
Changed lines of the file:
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@@
 <part name="R33" library="OSSI" deviceset="R" device="0603(1608)" value="4.7k"/>
 <part name="R37" library="OSSI" deviceset="R" device="0603(1608)" value="1.5k"/>
-<part name="C8" library="OSSI" deviceset="C" device="0603(1608)" value="1500pF"/>
-<part name="L5" library="OSSI" deviceset="L" device="0603(1608)" value="47nH"/>
+<part name="C8" library="OSSI" deviceset="C" device="0603(1608)" value="1000pF"/>
+<part name="L5" library="OSSI" deviceset="L" device="0603(1608)" value="39nH"/>
 <part name="GND9" library="OSSI" deviceset="GND" device=""/>
 <part name="C7" library="OSSI" deviceset="C" device="0805(2012)" value="470pF 0805"/>
 <part name="C6" library="OSSI" deviceset="C" device="1206(3216)-GCM31" value="10uF"/>
-<part name="C4" library="OSSI" deviceset="C" device="0603(1608)" value="15pF"/>
+<part name="C4" library="OSSI" deviceset="C" device="0603(1608)" value="8.2pF"/>
 <part name="GND10" library="OSSI" deviceset="GND" device=""/>
 <part name="F1" library="OSSI" deviceset="LFCN-160" device="" value="LFCN-530"/>
@@
 <text x="73.66" y="236.22" size="1.778" layer="94" rot="R90">chage this if resistance affects</text>
 <text x="175.26" y="208.28" size="1.778" layer="94">pull down!!</text>
+<wire x1="111.76" y1="91.44" x2="111.76" y2="25.4" width="0.1524" layer="94" style="shortdash"/>
+<wire x1="111.76" y1="25.4" x2="205.74" y2="25.4" width="0.1524" layer="94" style="shortdash"/>
+<wire x1="205.74" y1="25.4" x2="205.74" y2="91.44" width="0.1524" layer="94" style="shortdash"/>
+<wire x1="205.74" y1="91.44" x2="111.76" y2="91.44" width="0.1524" layer="94" style="shortdash"/>
+<text x="147.32" y="30.48" size="1.778" layer="94">15.5dB Gain @ these values</text>
 </plain>
 <instances>
@@
 <instance part="C7" gate="G$1" x="137.16" y="63.5"/>
 <instance part="C6" gate="G$1" x="129.54" y="63.5"/>
-<instance part="C4" gate="G$1" x="137.16" y="53.34" rot="R90"/>
+<instance part="C4" gate="G$1" x="116.84" y="53.34" rot="R90"/>
 <instance part="GND10" gate="1" x="127" y="55.88" rot="R270"/>
 <instance part="F1" gate="G$1" x="223.52" y="63.5" rot="R180"/>
@@
 <pinref part="C4" gate="G$1" pin="2"/>
 <pinref part="U1" gate="G$1" pin="4"/>
-<wire x1="142.24" y1="53.34" x2="149.86" y2="53.34" width="0.1524" layer="91"/>
+<wire x1="121.92" y1="53.34" x2="149.86" y2="53.34" width="0.1524" layer="91"/>
 </segment>
 </net>
@@
 <pinref part="C4" gate="G$1" pin="1"/>
 <pinref part="L3" gate="G$1" pin="2"/>
-<wire x1="134.62" y1="53.34" x2="104.14" y2="53.34" width="0.1524" layer="91"/>
+<wire x1="114.3" y1="53.34" x2="104.14" y2="53.34" width="0.1524" layer="91"/>
 <pinref part="L2" gate="G$1" pin="1"/>
 <wire x1="104.14" y1="53.34" x2="101.6" y2="53.34" width="0.1524" layer="91"/>

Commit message: LNA values
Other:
- note added: "15.5dB Gain Measured @ these values"
- note added: "15pF / 47nH / 1500pF will give similar results"
- note removed: "15.5dB Gain @ these values"
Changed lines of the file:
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@@
 <wire x1="205.74" y1="25.4" x2="205.74" y2="91.44" width="0.1524" layer="94" style="shortdash"/>
 <wire x1="205.74" y1="91.44" x2="111.76" y2="91.44" width="0.1524" layer="94" style="shortdash"/>
-<text x="147.32" y="30.48" size="1.778" layer="94">15.5dB Gain @ these values</text>
+<text x="147.32" y="30.48" size="1.778" layer="94">15.5dB Gain Measured @ these values</text>
+<text x="147.32" y="27.94" size="1.778" layer="94">15pF / 47nH / 1500pF will give similar results</text>
 </plain>
 <instances>
